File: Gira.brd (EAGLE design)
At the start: 38 x 65 mm, 20 parts, among them IC1 MEGA8-PTQFP

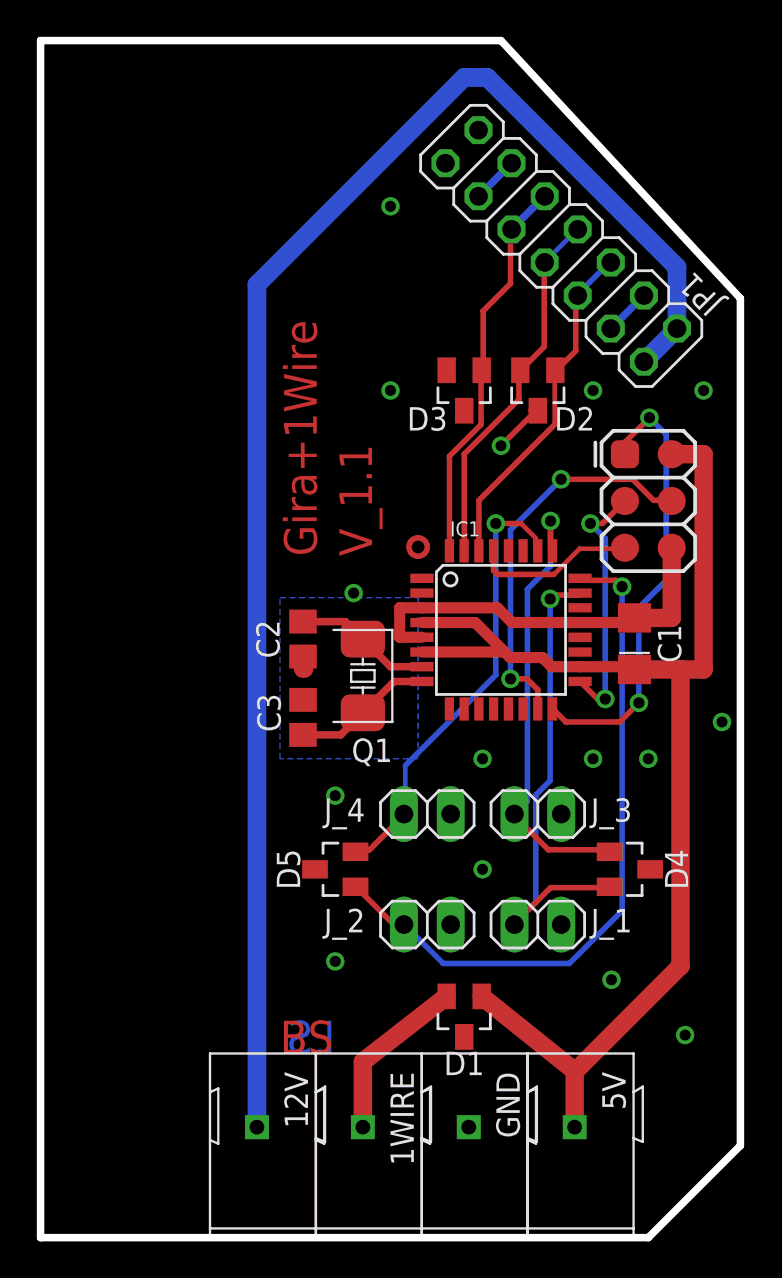
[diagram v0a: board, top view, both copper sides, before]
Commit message: Additional ground, I²C bus, input for light measurement
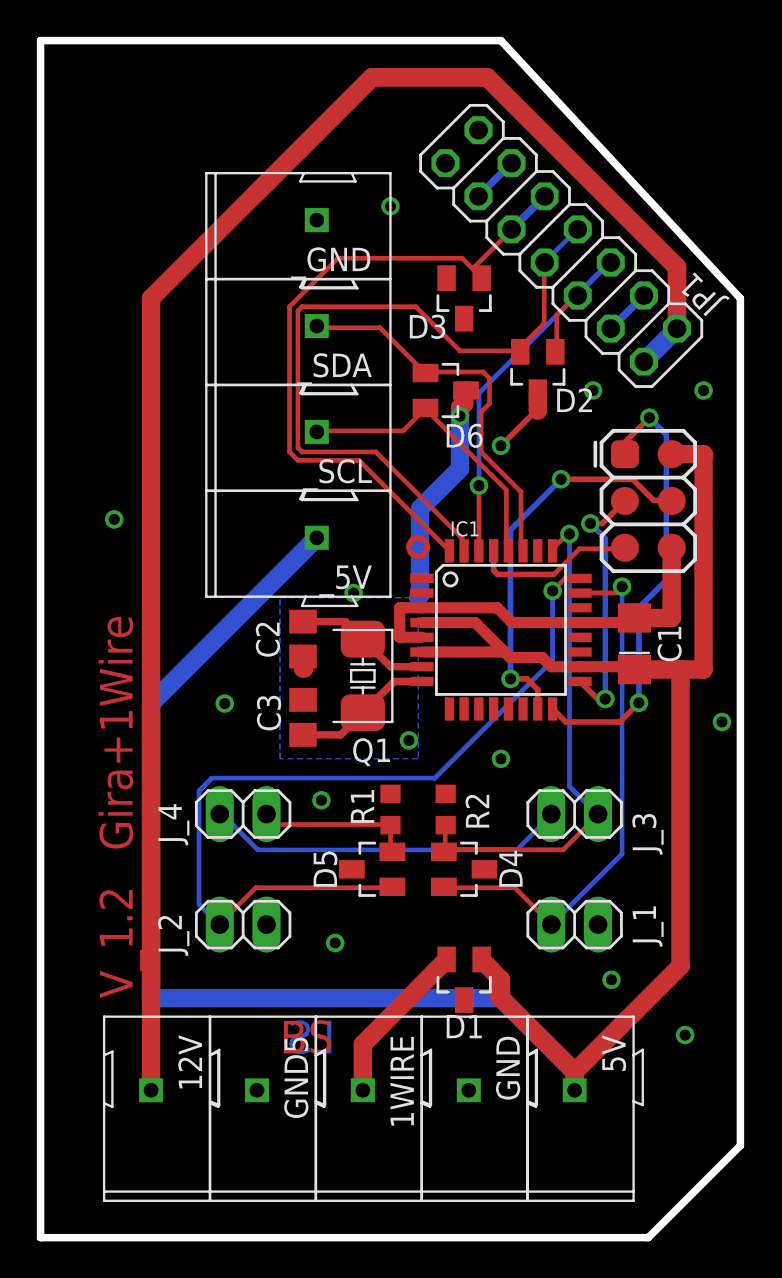
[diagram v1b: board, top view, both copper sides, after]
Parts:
- added D6: ESD_DIODES, common:SOT23
- added GND5, _5V, _GND, _SCL, _SDA: WAGO_243, common:WAGO_243
- added R1, R2: (no value), resistor:R0603
- moved J_2 10.0 mm to (16.0, 22.0)
- moved J_4 10.0 mm to (16.0, 28.0)
- moved D4 9.00 mm to (28.0, 25.0)
- moved 12V 6.09 mm to (11.0, 13.0)
- moved D3 5.00 mm to (28.0, 56.0)
- moved 1WIRE 2.00 mm to (22.5, 13.0)
- moved 5V 2.00 mm to (34.0, 13.0)
- moved D1 2.00 mm to (28.0, 19.0)
- moved D5 2.00 mm to (23.0, 25.0)
- moved GND 2.00 mm to (28.2, 13.0)
- moved J_1 2.00 mm to (34.0, 22.0)
- moved J_3 2.00 mm to (34.0, 28.0)
- moved D2 1.00 mm to (32.0, 52.0)
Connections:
- new net N$6: D5.2, J_4.2, R1.1
- new net SCL: D6.2, IC1.28, _SCL.P$1
- new net SDA: D6.1, IC1.27, _SDA.P$1
- new net VCC: J_3.1, J_4.1
- net 5V: now also _5V.P$1
- net B3: now also J_3.2, R2.1; no longer J_3.1
- net B4: no longer D5.2, J_4.1
- net GND: now also D6.3, GND5.P$1, R1.2, R2.2, _GND.P$1; no longer J_3.2, J_4.2
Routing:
- net 5V: track 68.0 -> 122.2 mm
- net B4: track 24.6 -> 0.00 mm, vias 1 -> 0
- net SDA: track 0.00 -> 21.2 mm
- net N$14: track 20.0 -> 40.3 mm
- net VCC: track 0.00 -> 19.7 mm
- net SCL: track 0.00 -> 16.1 mm
- net N$16: track 21.4 -> 37.0 mm
- net GND: track 27.3 -> 42.0 mm
- net N$6: track 0.00 -> 8.46 mm
- net B2: track 37.5 -> 45.7 mm
- net N$15: track 18.7 -> 22.3 mm, vias 0 -> 1
- net B3: track 24.5 -> 27.9 mm
- net N$12: track 83.4 -> 86.7 mm
- net B1: track 26.4 -> 29.1 mm
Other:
- board text added: "V_1.2"
- board text removed: "V_1.1"

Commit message: Update Gira
min 0.3mm
Klemmen gedreht
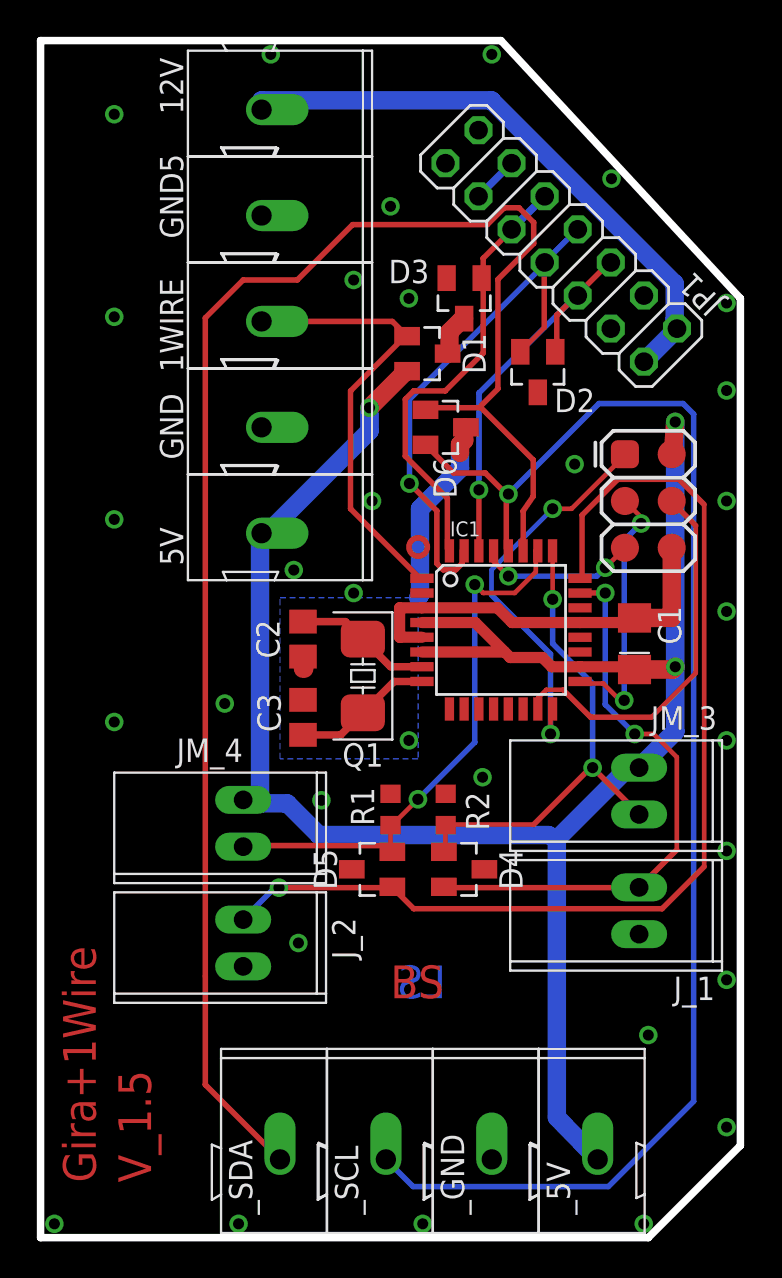
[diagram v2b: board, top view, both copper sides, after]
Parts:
- removed J_3, J_4: (no value), pinhead:1X02
- added JM_3, JM_4: (no value), common:1X02_GN
- J_1, J_2: device pinhead:1X02 -> common:1X02_GN
- moved 12V 53.6 mm to (17.0, 66.2), turned to 0 degrees
- moved _GND 51.9 mm to (29.5, 9.25), turned to 90 degrees
- moved GND5 47.5 mm to (17.0, 60.5), turned to 0 degrees
- moved _SDA 45.3 mm to (18.0, 9.25), turned to 90 degrees
- moved 1WIRE 42.1 mm to (17.0, 54.8), turned to 0 degrees
- moved _SCL 39.7 mm to (23.8, 9.25), turned to 90 degrees
- moved GND 37.7 mm to (17.0, 49.0), turned to 0 degrees
- moved _5V 37.0 mm to (35.2, 9.25), turned to 90 degrees
- moved 5V 34.7 mm to (17.0, 43.2), turned to 0 degrees
- moved D1 34.1 mm to (26.0, 53.0), turned to 270 degrees
- moved J_1 3.58 mm to (37.5, 22.8), turned to 90 degrees
- moved D6 2.00 mm to (27.0, 49.0)
- moved J_2 1.00 mm to (16.0, 21.0), turned to 90 degrees
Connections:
- removed net N$6: D5.2, J_4.2, R1.1
- removed net VCC: J_3.1, J_4.1
- net 5V: now also D1.2, JM_3.2, JM_4.2; no longer D1.1
- net B1: now also J_1.2; no longer J_1.1
- net B2: now also J_2.2; no longer J_2.1
- net B3: now also JM_3.1; no longer J_3.2
- net B4: now also D5.2, JM_4.1, R1.1
- net GND: now also J_1.1, J_2.1; no longer J_1.2, J_2.2
- net N$2: now also D1.1, IC1.1; no longer D1.2
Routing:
- net SDA: track 21.2 -> 91.5 mm
- net SCL: track 16.1 -> 77.6 mm, vias 0 -> 1
- net N$12: track 86.7 -> 32.1 mm
- net B4: track 0.00 -> 30.1 mm, vias 0 -> 2
- net VCC: track 19.7 -> 0.00 mm
- net N$2: track 8.97 -> 24.4 mm
- net B2: track 45.7 -> 58.4 mm
- net N$16: track 37.0 -> 24.5 mm
- net 5V: track 122.2 -> 110.7 mm, vias 0 -> 3
- net N$14: track 40.3 -> 30.4 mm, vias 0 -> 1
- net N$6: track 8.46 -> 0.00 mm
- net GND: track 42.0 -> 35.1 mm, vias 15 -> 32
- net N$9: track 24.6 -> 21.6 mm
- net B1: track 29.1 -> 31.0 mm, vias 1 -> 2
- net B3: track 27.9 -> 27.0 mm, vias 1 -> 2
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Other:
- board text added: "V_1.5"
- board text removed: "V_1.2"

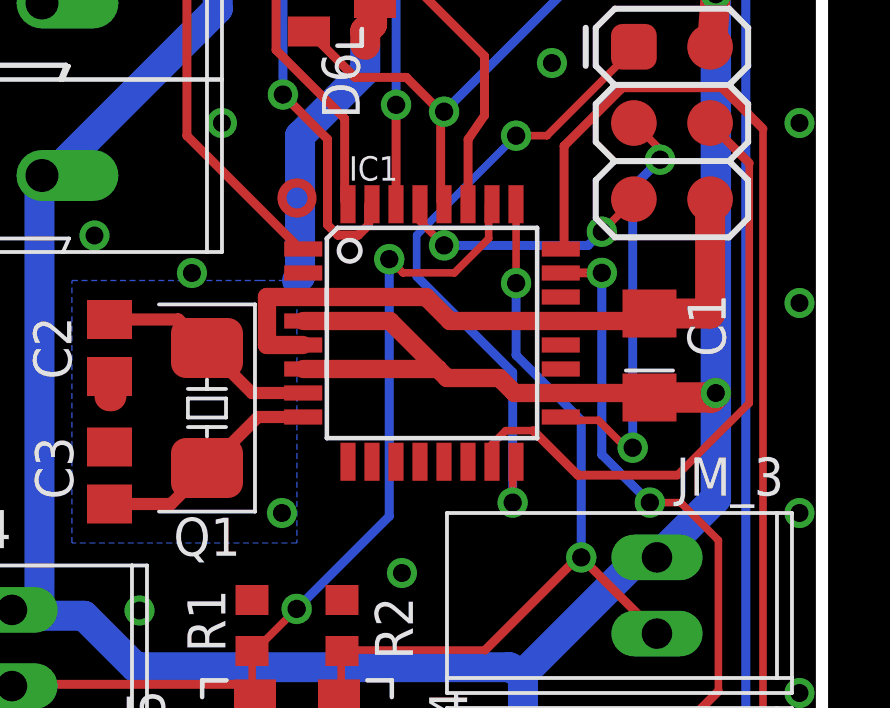
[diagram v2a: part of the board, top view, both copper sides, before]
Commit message: Gira: längere Pads für CPU
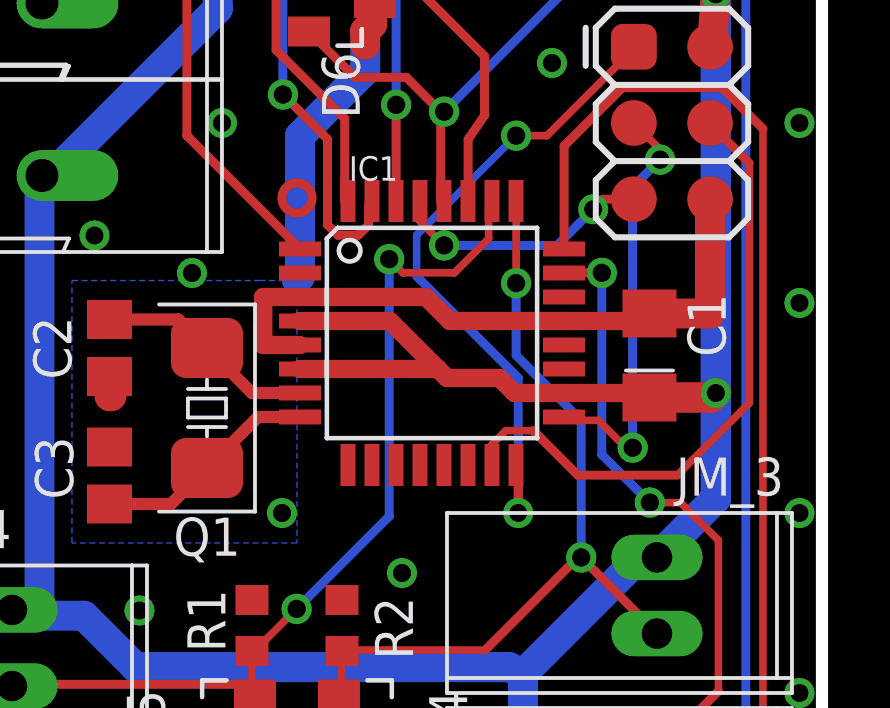
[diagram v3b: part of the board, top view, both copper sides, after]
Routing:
- net N$9: track 21.6 -> 22.3 mm

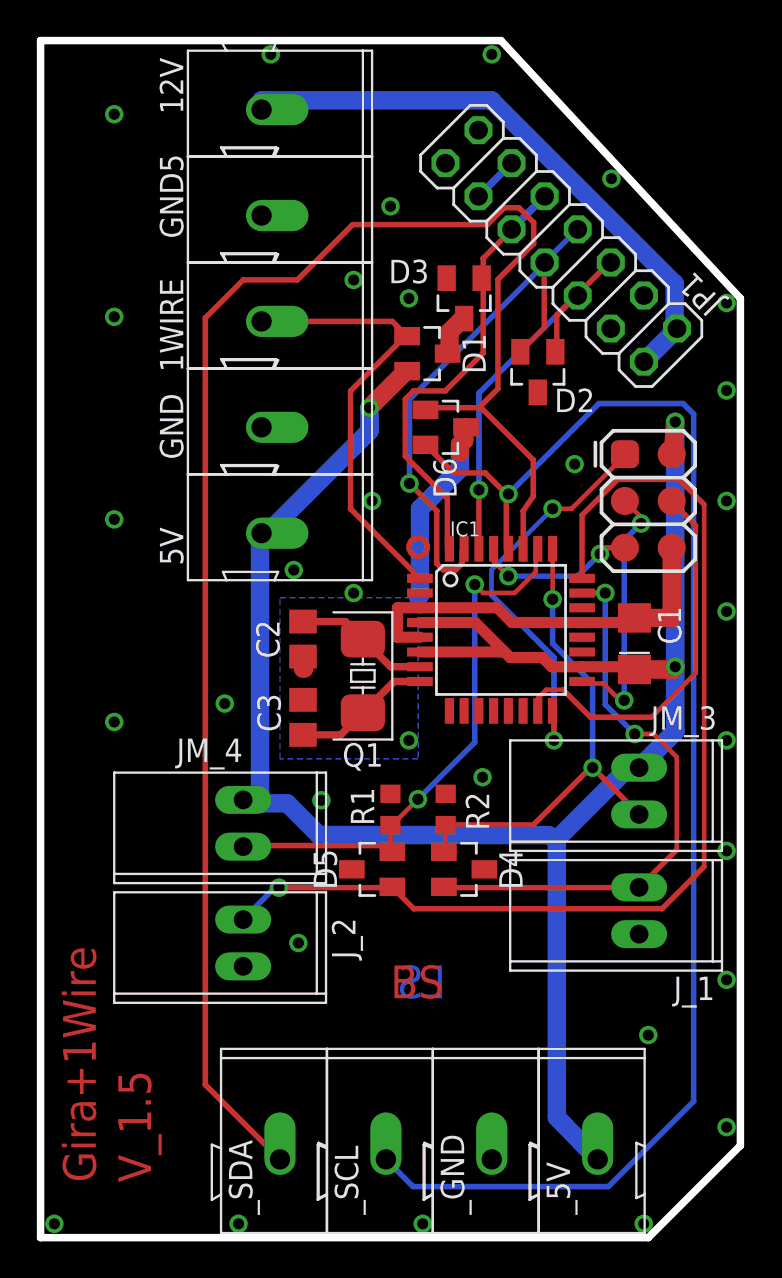
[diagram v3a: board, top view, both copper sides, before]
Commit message: V2.1
* Umstellung auf 3.3V (aus dem Rauchmelder)
* keine Pullups am Port
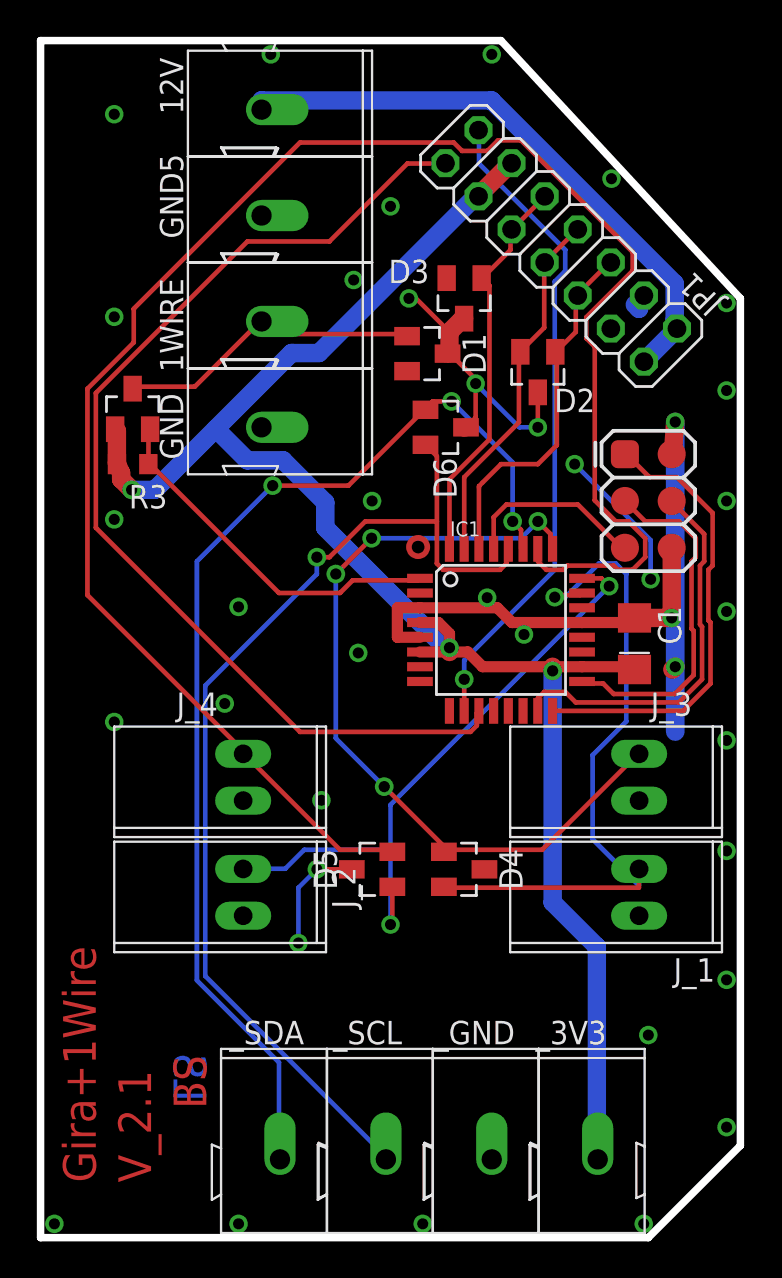
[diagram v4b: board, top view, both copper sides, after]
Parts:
- removed 5V: WAGO_243, common:WAGO_243
- removed C2, C3: CC0805, common:C0805
- removed JM_3, JM_4: (no value), common:1X02_GN
- removed Q1: (no value), common:Q_SMD5
- removed R1, R2: (no value), resistor:R0603
- added J_3, J_4: (no value), common:1X02_GN
- added Q2: 2N7002, common:SOT23
- added R3: (no value), common:R0603
- moved J_2 2.75 mm to (16.0, 23.8)
- moved J_1 1.00 mm to (37.5, 23.8)
- renumbered _5V to _3V3
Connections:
- removed net N$17: JP1.11, JP1.12
- removed net N$4: C3.2, IC1.8, Q1.P$1
- removed net N$5: C2.2, IC1.7, Q1.P$2
- new net 3V3: C1.+, IC1.18, IC1.4, IC1.6, JP1.11, JP1.12, Q2.1, R3.2, _3V3.P$1
- new net N$3: 1WIRE.P$1, D1.1, Q2.3
- new net RESET: IC1.10, JP1.13
- new net TEST: IC1.11, JP1.14
- net 5V: no longer 5V.P$1, C1.+, D1.2, IC1.18, IC1.4, IC1.6, JM_3.2, JM_4.2, _3V3.P$1
- net B3: now also J_3.2; no longer JM_3.1, R2.1
- net B4: now also J_4.2; no longer JM_4.1, R1.1
- net GND: now also J_3.1, J_4.1; no longer C2.1, C3.1, R1.2, R2.2
- net N$2: now also Q2.2, R3.1; no longer 1WIRE.P$1, D1.1
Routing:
- net 3V3: track 0.00 -> 92.7 mm, vias 0 -> 3
- net 5V: track 110.9 -> 19.0 mm, vias 3 -> 2
- net B4: track 30.1 -> 99.4 mm, vias 2 -> 0
- net TEST: track 0.00 -> 57.7 mm
- net RESET: track 0.00 -> 35.8 mm, vias 0 -> 1
- net SDA: track 91.4 -> 61.5 mm, vias 0 -> 3
- net B2: track 58.3 -> 35.5 mm, vias 1 -> 2
- net GND: track 35.2 -> 56.1 mm, vias 32 -> 37
- net SCL: track 77.6 -> 58.2 mm
- net B3: track 27.1 -> 44.5 mm, vias 2 -> 4
- net N$3: track 0.00 -> 16.8 mm
- net N$14: track 30.4 -> 19.9 mm, vias 1 -> 0
- net N$4: track 7.55 -> 0.00 mm
- net N$5: track 7.36 -> 0.00 mm
- net B1: track 30.9 -> 37.7 mm, vias 2 -> 1
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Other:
- board text added: "V_2.1"
- board text removed: "V_1.5"

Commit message: V 2.2
added Aref capacitor
fixed power supply via prog connector problem
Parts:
- added C2: (no value), common:CP1206
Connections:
- removed net 5V: U$1.P$2
- new net N$1: C2.+, IC1.20
- net 3V3: now also U$1.P$2
- net GND: now also C2.-
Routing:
- net B4: track 99.4 -> 35.4 mm, vias 0 -> 1
- net SDA: track 61.5 -> 121.2 mm, vias 3 -> 0
- net RESET: track 35.8 -> 61.1 mm, vias 1 -> 0
- net 5V: track 19.0 -> 0.00 mm, vias 2 -> 0
- net 3V3: track 92.7 -> 110.2 mm, vias 3 -> 5
- net B3: track 44.5 -> 28.8 mm, vias 4 -> 1
- net N$1: track 0.00 -> 12.7 mm, vias 0 -> 2
- net GND: track 56.1 -> 46.9 mm
- net B1: track 37.7 -> 29.4 mm
- net B2: track 35.5 -> 43.7 mm, vias 2 -> 3
- net SCL: track 58.2 -> 65.5 mm, vias 1 -> 2
- net N$16: track 21.7 -> 24.5 mm
- net N$10: track 19.1 -> 16.8 mm, vias 0 -> 2
- net N$11: track 10.2 -> 8.70 mm
- net N$15: track 19.8 -> 18.6 mm
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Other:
- board text added: "V_2.2"
- board text removed: "V_2.1"

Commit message: V2.2
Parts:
- removed D3: ESD_DIODES, common:SOT23
- removed GND: WAGO_243, common:WAGO_243
- added D7: ESD_DIODES, common:SOT23
- added Q1, Q3: 2N7002, common:SOT23
- added R1, R2: (no value), common:R0603
- added _SCL2, _SDA2: WAGO_243, common:WAGO_243
- moved _SDA 39.8 mm to (17.0, 49.0), turned to 0 degrees
- moved _SCL 34.7 mm to (17.0, 43.2), turned to 0 degrees
- moved C1 14.8 mm to (22.5, 37.9)
- moved C2 1.47 mm to (27.8, 30.1)
- moved D2 1.00 mm to (32.0, 53.0)
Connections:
- new net N$4: D7.1, Q3.3, _SDA2.P$1
- new net N$5: D7.2, Q1.3, _SCL2.P$1
- new net SCL2: IC1.28, Q1.2, R2.1
- new net SDA2: IC1.27, Q3.2, R1.1
- new net VCC: Q1.1, Q3.1, R1.2, R2.2
- net GND: now also D7.3; no longer D3.3, GND.P$1
- net N$16: now also D1.1, IC1.1; no longer D3.1, IC1.32
- net N$2: now also IC1.32; no longer IC1.1
- net N$3: now also D1.2; no longer D1.1
- net SCL: now also IC1.22; no longer IC1.28
- net SDA: now also IC1.19; no longer IC1.27
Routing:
- net SDA: track 121.2 -> 30.9 mm, vias 0 -> 2
- net SCL2: track 0.00 -> 43.0 mm, vias 0 -> 2
- net SCL: track 65.5 -> 33.3 mm
- net SDA2: track 0.00 -> 31.3 mm, vias 0 -> 2
- net GND: track 46.9 -> 27.1 mm, vias 37 -> 39
- net N$4: track 0.00 -> 17.7 mm
- net N$5: track 0.00 -> 16.0 mm
- net RESET: track 61.1 -> 49.9 mm, vias 0 -> 2
- net B4: track 35.4 -> 44.6 mm, vias 1 -> 2
- net VCC: track 0.00 -> 8.57 mm
- net B2: track 43.7 -> 35.7 mm
- net TEST: track 57.7 -> 50.5 mm, vias 0 -> 2
- net 3V3: track 110.2 -> 114.0 mm
- net N$16: track 24.5 -> 27.3 mm, vias 0 -> 4
- net N$2: track 19.3 -> 21.7 mm
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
